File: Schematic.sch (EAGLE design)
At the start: 21 parts, among them Q1 BC548, Q2 BC548, X1 20 Mhz

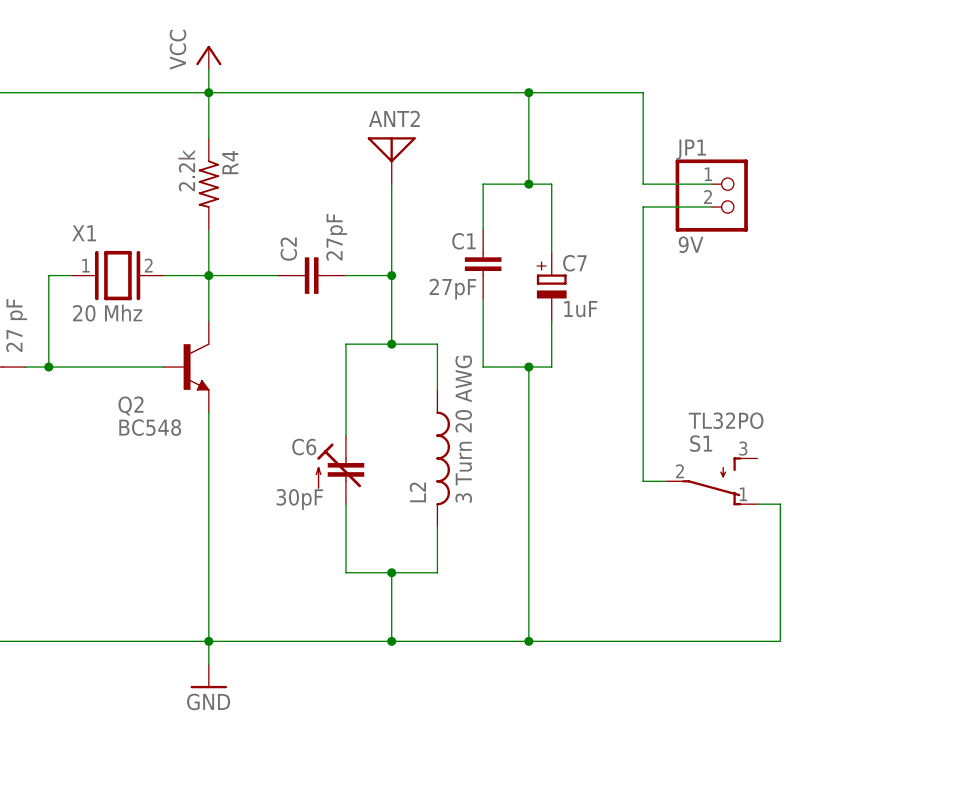
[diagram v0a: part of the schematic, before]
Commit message: Add PCB and more modifications
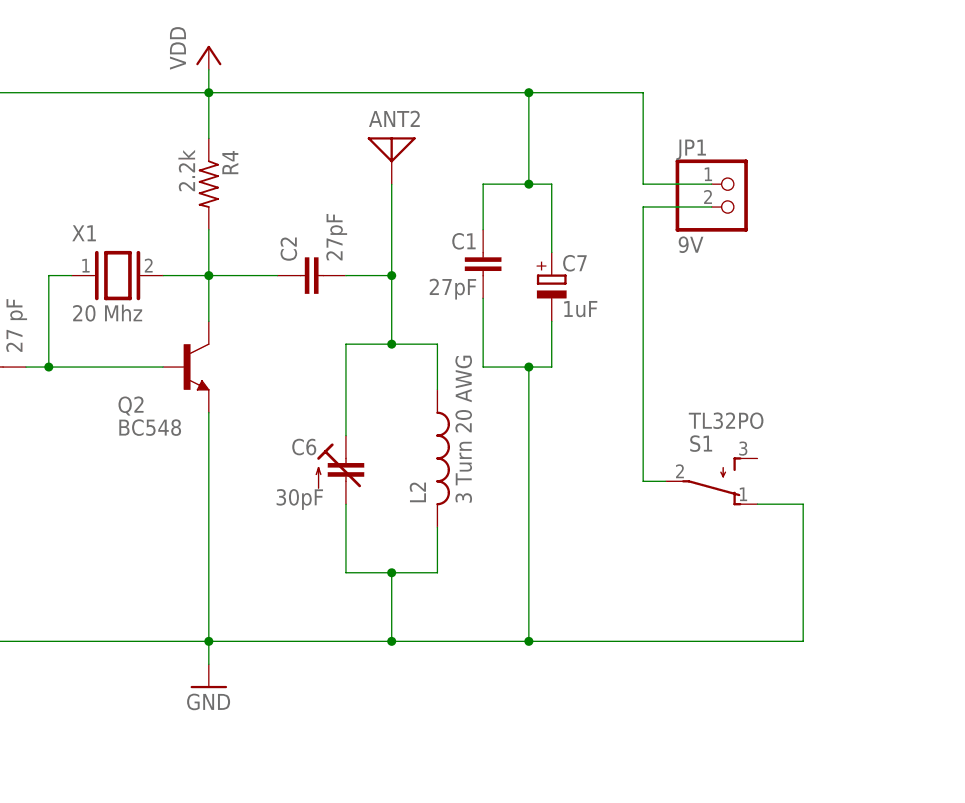
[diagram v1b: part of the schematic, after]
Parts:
- C5, C6: device c-trimm:C-TRIMM3008 -> resistor:C-TRIMM808
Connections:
- net N$1 renamed LED-
- net N$2 renamed ANT1
- net N$3 renamed CRYSTAL1
- net N$4 renamed CRYSTAL2
- net N$5 renamed L4TURN
- net N$7 renamed BAT-
- net N$8 renamed ANT2
- net VCC renamed VDD
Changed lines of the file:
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@@
 <part name="ANT2" library="discrete" library_urn="urn:adsk.eagle:library:211" deviceset="ANTENNA" device="" package3d_urn="urn:adsk.eagle:package:12928/1"/>
 <part name="LED1" library="led" library_urn="urn:adsk.eagle:library:259" deviceset="LED" device="3MM" package3d_urn="urn:adsk.eagle:package:15797/1"/>
-<part name="P+1" library="supply1" library_urn="urn:adsk.eagle:library:371" deviceset="VCC" device=""/>
+<part name="P+1" library="supply1" library_urn="urn:adsk.eagle:library:371" deviceset="VCC" device="" value="VDD"/>
 <part name="JP1" library="pinhead" library_urn="urn:adsk.eagle:library:325" deviceset="PINHD-1X2" device="" package3d_urn="urn:adsk.eagle:package:22435/2" value="9V"/>
 <part name="C1" library="capacitor-wima" library_urn="urn:adsk.eagle:library:116" deviceset="C" device="2,5-3" package3d_urn="urn:adsk.eagle:package:5436/1" value="27pF"/>
@@
 <part name="X1" library="special" library_urn="urn:adsk.eagle:library:367" deviceset="XTAL/S" device="" package3d_urn="urn:adsk.eagle:package:26647/2" value="20 Mhz"/>
 <part name="L1" library="rcl" library_urn="urn:adsk.eagle:library:334" deviceset="L-US" device="0204/5" package3d_urn="urn:adsk.eagle:package:23488/1" value="4 Turn 20 AWG"/>
-<part name="C5" library="c-trimm" library_urn="urn:adsk.eagle:library:114" deviceset="C-TRIMM" device="3008" package3d_urn="urn:adsk.eagle:package:5346/1" value="30pF"/>
-<part name="C6" library="c-trimm" library_urn="urn:adsk.eagle:library:114" deviceset="C-TRIMM" device="3008" package3d_urn="urn:adsk.eagle:package:5346/1" value="30pF"/>
+<part name="C5" library="resistor" library_urn="urn:adsk.eagle:library:348" deviceset="C-TRIMM" device="808" package3d_urn="urn:adsk.eagle:package:23766/1" value="30pF"/>
+<part name="C6" library="resistor" library_urn="urn:adsk.eagle:library:348" deviceset="C-TRIMM" device="808" package3d_urn="urn:adsk.eagle:package:23766/1" value="30pF"/>
 <part name="L2" library="rcl" library_urn="urn:adsk.eagle:library:334" deviceset="L-US" device="0204/5" package3d_urn="urn:adsk.eagle:package:23488/1" value="3 Turn 20 AWG"/>
 <part name="GND1" library="supply1" library_urn="urn:adsk.eagle:library:371" deviceset="GND" device=""/>
@@
 </busses>
 <nets>
-<net name="N$1" class="0">
+<net name="LED-" class="0">
 <segment>
 <pinref part="LED1" gate="G$1" pin="C"/>
@@
 </segment>
 </net>
-<net name="N$2" class="0">
+<net name="ANT1" class="0">
 <segment>
 <pinref part="R2" gate="G$1" pin="2"/>
@@
 </segment>
 </net>
-<net name="N$3" class="0">
+<net name="CRYSTAL1" class="0">
 <segment>
 <pinref part="C4" gate="G$1" pin="2"/>
@@
 </segment>
 </net>
-<net name="N$4" class="0">
+<net name="CRYSTAL2" class="0">
 <segment>
 <pinref part="X1" gate="G$1" pin="2"/>
@@
 </segment>
 </net>
-<net name="N$5" class="0">
+<net name="L4TURN" class="0">
 <segment>
 <pinref part="C3" gate="G$1" pin="2"/>
@@
 </segment>
 </net>
-<net name="VCC" class="0">
+<net name="VDD" class="0">
 <segment>
 <pinref part="P+1" gate="VCC" pin="VCC"/>
@@
 </segment>
 </net>
-<net name="N$8" class="0">
+<net name="ANT2" class="0">
 <segment>
 <pinref part="ANT2" gate="A" pin="1"/>
@@
 <wire x1="144.78" y1="15.24" x2="129.54" y2="15.24" width="0.1524" layer="91"/>
 <junction x="129.54" y="15.24"/>
+<wire x1="144.78" y1="15.24" x2="175.26" y2="15.24" width="0.1524" layer="91"/>
+<junction x="144.78" y="15.24"/>
 <pinref part="S1" gate="BEF1" pin="O"/>
-<wire x1="170.18" y1="30.48" x2="172.72" y2="30.48" width="0.1524" layer="91"/>
-<wire x1="172.72" y1="30.48" x2="172.72" y2="15.24" width="0.1524" layer="91"/>
-<wire x1="172.72" y1="15.24" x2="144.78" y2="15.24" width="0.1524" layer="91"/>
-<junction x="144.78" y="15.24"/>
-</segment>
-</net>
-<net name="N$7" class="0">
+<wire x1="175.26" y1="15.24" x2="175.26" y2="30.48" width="0.1524" layer="91"/>
+<wire x1="175.26" y1="30.48" x2="170.18" y2="30.48" width="0.1524" layer="91"/>
+</segment>
+</net>
+<net name="BAT-" class="0">
 <segment>
 <pinref part="JP1" gate="G$1" pin="2"/>
